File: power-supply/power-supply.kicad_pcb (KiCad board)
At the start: 2 copper layers, 105 x 46.5 mm, 23 parts, among them J1 Barrel_Jack_Switch, J2 Output, U1 LM7812_TO220, U2 LM7912_TO220

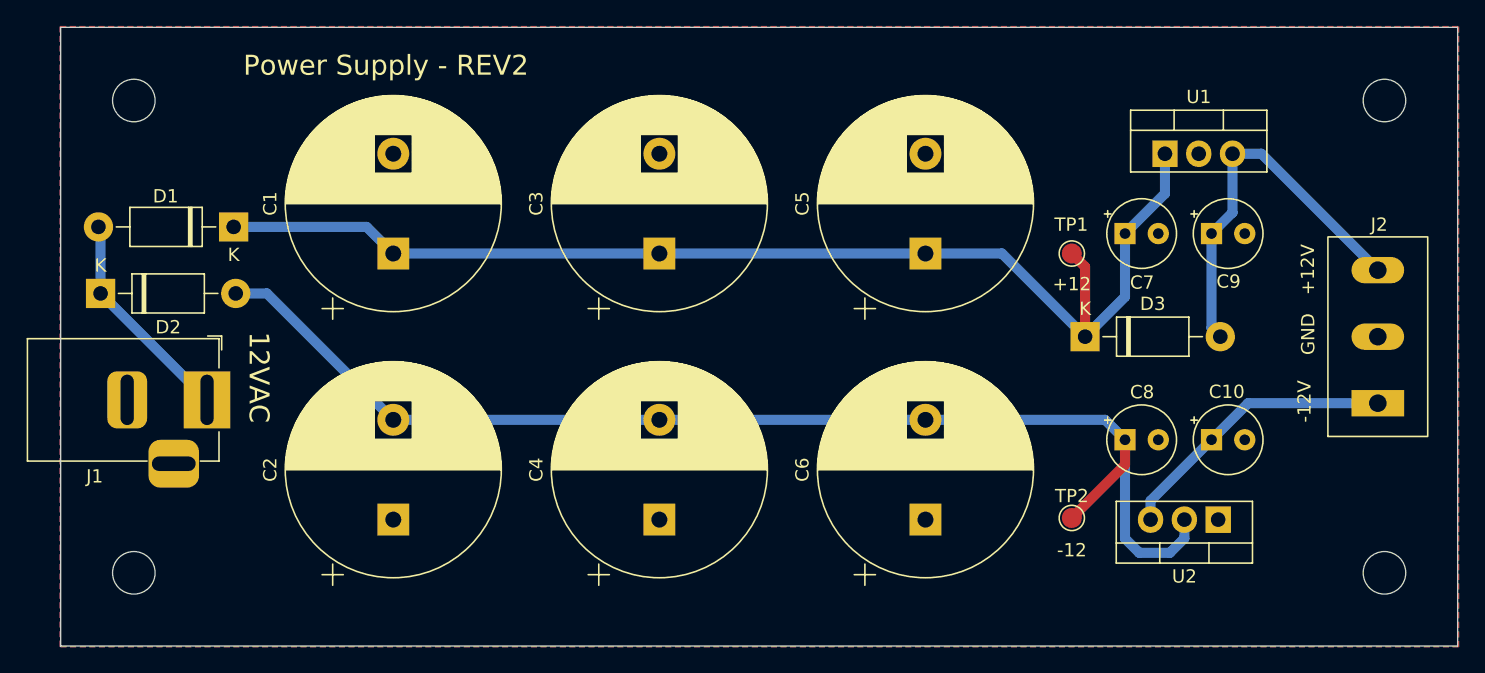
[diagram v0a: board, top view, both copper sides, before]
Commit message: Fixed capacitor polarity on power supply
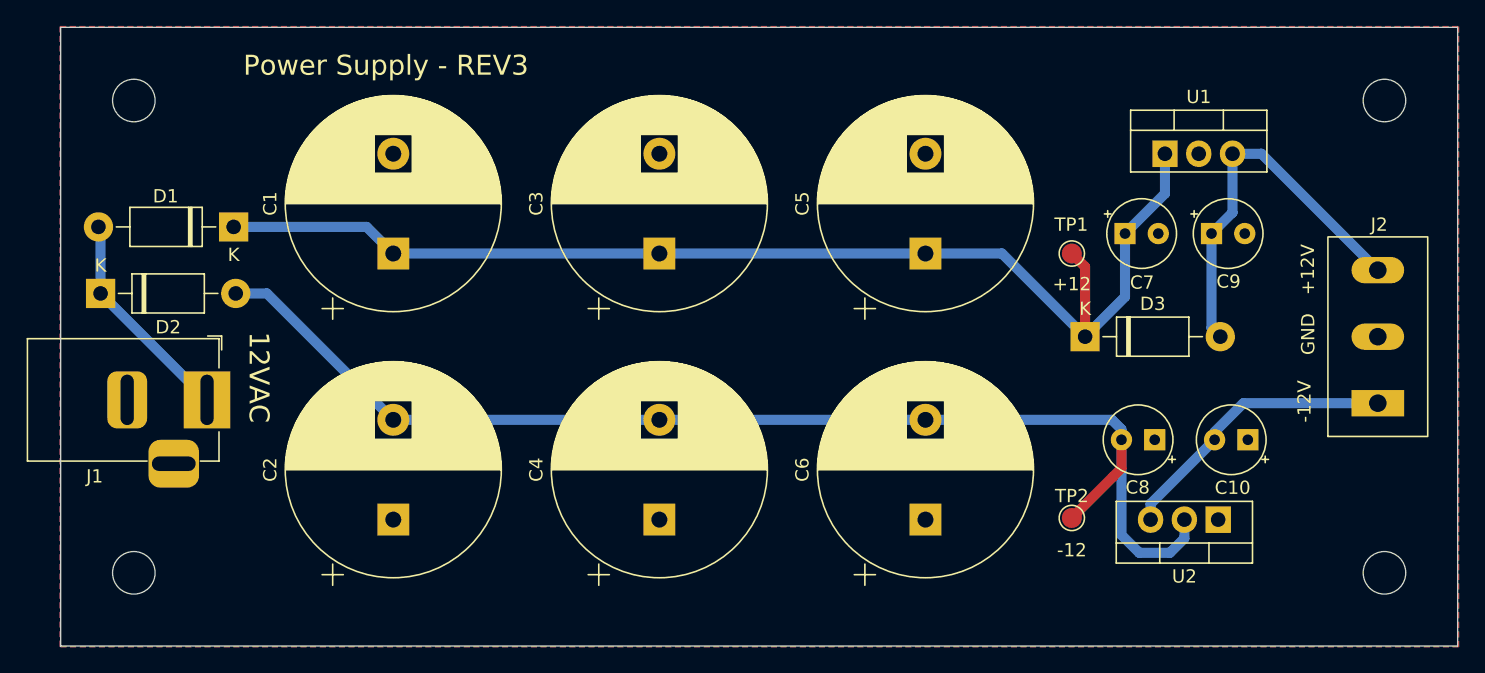
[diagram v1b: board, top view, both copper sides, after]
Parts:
- moved C10 2.73 mm to (174.2, 99.0), turned to 180 degrees
- moved C8 2.23 mm to (167.2, 99.0), turned to 180 degrees
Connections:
- C10 pad 1: Net-(C10-Pad1) -> GND
- C10 pad 2: GND -> Net-(C10-Pad2)
- C8 pad 1: Net-(C2-Pad2) -> GND
- C8 pad 2: GND -> Net-(C2-Pad2)
- J2 pad 1: Net-(C10-Pad1) -> Net-(C10-Pad2)
- U2 pad 3: Net-(C10-Pad1) -> Net-(C10-Pad2)
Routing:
- net Net-(C10-Pad2): track 0.00 -> 21.7 mm
- net Net-(C10-Pad1): track 21.5 -> 0.00 mm
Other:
- board text added: "Power Supply - REV3"
- board text removed: "Power Supply - REV2"
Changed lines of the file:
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@@
   (net 3 "Net-(C2-Pad2)")
   (net 4 "Net-(C9-Pad1)")
-  (net 5 "Net-(C10-Pad1)")
+  (net 5 "Net-(C10-Pad2)")
   (net 6 "Net-(D1-Pad2)")
   (net 7 "unconnected-(J1-Pad3)")
@@
     (fp_rect (start -7.5 -3.75) (end 7.5 3.75) (layer "F.SilkS") (width 0.12) (fill none))
     (pad "1" thru_hole rect (at -5 0 90) (size 1.98 3.96) (drill 1.32) (layers *.Cu *.Mask)
-      (net 5 "Net-(C10-Pad1)") (pinfunction "Pin_1") (pintype "passive"))
+      (net 5 "Net-(C10-Pad2)") (pinfunction "Pin_1") (pintype "passive"))
     (pad "2" thru_hole oval (at 0 0 90) (size 1.98 3.96) (drill 1.32) (layers *.Cu *.Mask)
       (net 2 "GND") (pinfunction "Pin_2") (pintype "passive"))
@@
       (net 3 "Net-(C2-Pad2)") (pinfunction "VI") (pintype "power_in"))
     (pad "3" thru_hole oval (at 5.08 0 180) (size 1.905 2) (drill 1.1) (layers *.Cu *.Mask)
-      (net 5 "Net-(C10-Pad1)") (pinfunction "VO") (pintype "power_out"))
+      (net 5 "Net-(C10-Pad2)") (pinfunction "VO") (pintype "power_out"))
     (model "${KICAD6_3DMODEL_DIR}/Package_TO_SOT_THT.3dshapes/TO-220-3_Vertical.wrl"
       (offset (xyz 0 0 0))
@@
   )
   (footprint "Capacitor_THT:CP_Radial_Tantal_D5.0mm_P2.50mm" (layer "F.Cu")
-    (at 165 99)
+    (at 167.232 99 180)
     (descr "CP, Radial_Tantal series, Radial, pin pitch=2.50mm, , diameter=5.0mm, Tantal Electrolytic Capacitor, http://cdn-reichelt.de/documents/datenblatt/B300/TANTAL-TB-Serie%23.pdf")
     (tags "CP Radial_Tantal series Radial pin pitch 2.50mm  diameter 5.0mm Tantal Electrolytic Capacitor")
@@
     (fp_line (start -0.883605 -1.0875) (end -0.383605 -1.0875) (layer "F.Fab") (width 0.1))
     (fp_circle (center 1.25 0) (end 3.75 0) (layer "F.Fab") (width 0.1) (fill none))
-    (pad "1" thru_hole rect (at 0 0) (size 1.6 1.6) (drill 0.8) (layers *.Cu *.Mask)
+    (pad "1" thru_hole rect (at 0 0 180) (size 1.6 1.6) (drill 0.8) (layers *.Cu *.Mask)
+      (net 2 "GND") (pintype "passive"))
+    (pad "2" thru_hole circle (at 2.5 0 180) (size 1.6 1.6) (drill 0.8) (layers *.Cu *.Mask)
       (net 3 "Net-(C2-Pad2)") (pintype "passive"))
-    (pad "2" thru_hole circle (at 2.5 0) (size 1.6 1.6) (drill 0.8) (layers *.Cu *.Mask)
-      (net 2 "GND") (pintype "passive"))
     (model "${KICAD6_3DMODEL_DIR}/Capacitor_THT.3dshapes/CP_Radial_Tantal_D5.0mm_P2.50mm.wrl"
       (offset (xyz 0 0 0))
@@
   )
   (footprint "Capacitor_THT:CP_Radial_Tantal_D5.0mm_P2.50mm" (layer "F.Cu")
-    (at 171.5 99)
+    (at 174.232 99 180)
     (descr "CP, Radial_Tantal series, Radial, pin pitch=2.50mm, , diameter=5.0mm, Tantal Electrolytic Capacitor, http://cdn-reichelt.de/documents/datenblatt/B300/TANTAL-TB-Serie%23.pdf")
     (tags "CP Radial_Tantal series Radial pin pitch 2.50mm  diameter 5.0mm Tantal Electrolytic Capacitor")
@@
     (property "Supplier Part No." "A-265 ")
     (attr through_hole)
-    (fp_text reference "C10" (at 1.143 -3.6068 180) (layer "F.SilkS")
+    (fp_text reference "C10" (at 1.143 -3.6068) (layer "F.SilkS")
       (effects (font (size 1 1) (thickness 0.15)))
     )
@@
     (fp_line (start -0.633605 -1.3375) (end -0.633605 -0.8375) (layer "F.Fab") (width 0.1))
     (fp_circle (center 1.25 0) (end 3.75 0) (layer "F.Fab") (width 0.1) (fill none))
-    (pad "1" thru_hole rect (at 0 0) (size 1.6 1.6) (drill 0.8) (layers *.Cu *.Mask)
-      (net 5 "Net-(C10-Pad1)") (pintype "passive"))
-    (pad "2" thru_hole circle (at 2.5 0) (size 1.6 1.6) (drill 0.8) (layers *.Cu *.Mask)
+    (pad "1" thru_hole rect (at 0 0 180) (size 1.6 1.6) (drill 0.8) (layers *.Cu *.Mask)
       (net 2 "GND") (pintype "passive"))
+    (pad "2" thru_hole circle (at 2.5 0 180) (size 1.6 1.6) (drill 0.8) (layers *.Cu *.Mask)
+      (net 5 "Net-(C10-Pad2)") (pintype "passive"))
     (model "${KICAD6_3DMODEL_DIR}/Capacitor_THT.3dshapes/CP_Radial_Tantal_D5.0mm_P2.50mm.wrl"
       (offset (xyz 0 0 0))
@@
     (effects (font (size 1 1) (thickness 0.15)))
   )
-  (gr_text "Power Supply - REV2" (at 109.4486 70.866) (layer "F.SilkS")
+  (gr_text "Power Supply - REV3" (at 109.4486 70.866) (layer "F.SilkS")
     (effects (font (size 1.5 1.5) (thickness 0.3)))
   )
@@
   (segment (start 165 83.5) (end 165 88.25) (width 0.76) (layer "B.Cu") (net 1))
   (segment (start 130 85) (end 150 85) (width 0.76) (layer "B.Cu") (net 1))
-  (segment (start 165 99) (end 165 100.8766) (width 0.76) (layer "F.Cu") (net 3))
-  (segment (start 165 100.8766) (end 161 104.8766) (width 0.76) (layer "F.Cu") (net 3))
-  (segment (start 165 99) (end 165 106.4276) (width 0.76) (layer "B.Cu") (net 3))
-  (segment (start 165 106.4276) (end 166.0652 107.4928) (width 0.76) (layer "B.Cu") (net 3))
-  (segment (start 150 97.5) (end 163.5 97.5) (width 0.76) (layer "B.Cu") (net 3))
+  (segment (start 164.0973 101.7793) (end 161 104.8766) (width 0.76) (layer "F.Cu") (net 3))
+  (segment (start 164.732 99) (end 164.732 101.1446) (width 0.76) (layer "F.Cu") (net 3))
+  (segment (start 164.732 101.1446) (end 164.0973 101.7793) (width 0.76) (layer "F.Cu") (net 3))
+  (segment (start 164.018 97.5) (end 164.732 98.214) (width 0.76) (layer "B.Cu") (net 3))
+  (segment (start 169.46 106.4094) (end 169.46 105) (width 0.76) (layer "B.Cu") (net 3))
+  (segment (start 164.732 106.1596) (end 166.0652 107.4928) (width 0.76) (layer "B.Cu") (net 3))
+  (segment (start 164.732 99) (end 164.732 106.1596) (width 0.76) (layer "B.Cu") (net 3))
+  (segment (start 164.732 98.214) (end 164.732 99) (width 0.76) (layer "B.Cu") (net 3))
   (segment (start 110 97.5) (end 100.5 88) (width 0.76) (layer "B.Cu") (net 3))
   (segment (start 168.3766 107.4928) (end 169.46 106.4094) (width 0.76) (layer "B.Cu") (net 3))
@@
   (segment (start 100.5 88) (end 98.16 88) (width 0.76) (layer "B.Cu") (net 3))
   (segment (start 110 97.5) (end 130 97.5) (width 0.76) (layer "B.Cu") (net 3))
-  (segment (start 163.5 97.5) (end 165 99) (width 0.76) (layer "B.Cu") (net 3))
+  (segment (start 150 97.5) (end 164.018 97.5) (width 0.76) (layer "B.Cu") (net 3))
   (segment (start 166.0652 107.4928) (end 168.3766 107.4928) (width 0.76) (layer "B.Cu") (net 3))
-  (segment (start 169.46 106.4094) (end 169.46 105) (width 0.76) (layer "B.Cu") (net 3))
   (segment (start 171.5 83.5) (end 171.5 90.59) (width 0.76) (layer "B.Cu") (net 4))
   (segment (start 173.08 77.5) (end 175.25 77.5) (width 0.76) (layer "B.Cu") (net 4))
@@
   (segment (start 173.08 81.92) (end 171.5 83.5) (width 0.76) (layer "B.Cu") (net 4))
   (segment (start 173.08 77.5) (end 173.08 81.92) (width 0.76) (layer "B.Cu") (net 4))
-  (segment (start 166.92 105) (end 166.92 103.58) (width 0.76) (layer "B.Cu") (net 5))
-  (segment (start 166.92 103.58) (end 171.5 99) (width 0.76) (layer "B.Cu") (net 5))
-  (segment (start 174.25 96.25) (end 171.5 99) (width 0.76) (layer "B.Cu") (net 5))
-  (segment (start 184 96.25) (end 174.25 96.25) (width 0.76) (layer "B.Cu") (net 5))
+  (segment (start 166.92 103.812) (end 171.732 99) (width 0.76) (layer "B.Cu") (net 5))
+  (segment (start 173.896 96.25) (end 171.732 98.414) (width 0.76) (layer "B.Cu") (net 5))
+  (segment (start 184 96.25) (end 173.896 96.25) (width 0.76) (layer "B.Cu") (net 5))
+  (segment (start 166.92 105) (end 166.92 103.812) (width 0.76) (layer "B.Cu") (net 5))
+  (segment (start 171.732 98.414) (end 171.732 99) (width 0.76) (layer "B.Cu") (net 5))
   (segment (start 88 88) (end 88 83.16) (width 0.76) (layer "B.Cu") (net 6))
   (segment (start 88 83.16) (end 87.84 83) (width 0.76) (layer "B.Cu") (net 6))
